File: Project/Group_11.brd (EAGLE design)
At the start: 100 x 80 mm, 29 parts, among them J1 POWER_JACKPTH_LOCK, U1 +12v

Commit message: Modifica symbols e schematico aggiornato
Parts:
- moved R1 61.4 mm to (20.3, 20.3)
- moved D1 56.2 mm to (21.6, 24.1)
- moved R11 36.1 mm to (38.1, 22.9), turned to 90 degrees
- moved U2 35.8 mm to (43.2, 21.6)
- moved R10 34.2 mm to (33.0, 22.9), turned to 180 degrees
- moved R6 29.2 mm to (49.5, 55.9), turned to 180 degrees
- moved U$3 21.7 mm to (33.0, 63.5), turned to 0 degrees
- moved U$1 21.6 mm to (63.5, 67.3)
- moved R8 19.8 mm to (52.1, 71.1)
- moved R5 18.1 mm to (2.54, 44.5), turned to 270 degrees
- moved J6 17.3 mm to (68.6, 22.9)
- moved U$2 17.3 mm to (50.8, 39.4)
- moved R9 12.7 mm to (10.2, 44.5)
- moved S1 10.2 mm to (62.2, 14.0)
- moved C1 9.92 mm to (40.6, 11.4)
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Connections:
- new net N$17: J6.1, U$2.32
- new net N$18: C3.2, U$3.12
- net 5V: now also R2.2, R3.2, R8.2, R9.2; no longer R2.1, R3.1, R8.1, R9.1
- net GND: no longer C3.2, U$3.12
- net I2C_SCL_0: now also R2.1; no longer R2.2
- net I2C_SCL_1: now also R8.1; no longer R8.2
- net I2C_SDA: no longer J6.1, U$2.32
- net I2C_SDA_0: now also R3.1; no longer R3.2
- net I2C_SDA_1: now also R9.1; no longer R9.2
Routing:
- net PHOTO_OUT: track 0.00 -> 7.66 mm
- net TEMP_OUT: track 0.00 -> 5.50 mm
- net N$7: track 0.00 -> 5.08 mm
- net N$5: track 0.00 -> 5.08 mm
- net N$17: track 0.00 -> 5.08 mm
- net N$8: track 0.00 -> 4.83 mm
- net N$6: track 0.00 -> 4.83 mm
- net N$4: track 0.00 -> 4.83 mm
- net N$2: track 0.00 -> 4.24 mm
- net N$3: track 0.00 -> 3.91 mm

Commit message: Aggiornamento board
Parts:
- moved J2 62.2 mm to (78.7, 58.4), turned to 271.5 degrees
- moved C2 57.5 mm to (55.9, 17.8)
- moved J3 32.4 mm to (50.8, 61.0), turned to 90 degrees
- moved U1 31.9 mm to (52.1, 10.2)
- moved R5 27.4 mm to (27.9, 54.6)
- moved R9 26.2 mm to (34.3, 54.6)
- moved J7 26.2 mm to (61.0, 53.3)
- moved R4 25.4 mm to (73.7, 62.2)
- moved R3 24.4 mm to (73.7, 58.4)
- moved R7 24.1 mm to (54.6, 54.6), turned to 270 degrees
- moved R2 22.7 mm to (73.7, 54.6), turned to 180 degrees
- moved J8 21.6 mm to (24.1, 61.0)
- moved J5 18.1 mm to (61.0, 59.7), turned to 270 degrees
- moved J4 17.3 mm to (61.0, 66.0), turned to 270 degrees
- moved C1 13.5 mm to (49.5, 21.6)
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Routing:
- net PHOTO_OUT: track 7.66 -> 10.6 mm
- net TEMP_OUT: track 5.50 -> 8.04 mm
- net N$2: track 4.24 -> 2.31 mm
- added copper zone on layer 1, net GND

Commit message: Aggiornamento parte inferiore
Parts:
- moved U1 62.4 mm to (47.0, 72.4)
- moved C2 58.4 mm to (54.6, 76.2)
- moved S1 54.6 mm to (63.5, 72.4)
- moved J1 54.6 mm to (88.9, 72.4)
- moved C3 53.3 mm to (31.8, 67.3)
- moved C1 46.6 mm to (40.6, 67.3)
- moved J8 18.2 mm to (40.6, 53.3), turned to 180 degrees
- moved J7 15.3 mm to (45.7, 54.6)
- moved U$3 9.67 mm to (33.0, 58.4), turned to 0 degrees
- moved R5 8.52 mm to (31.8, 62.2)
- moved R9 8.13 mm to (39.4, 61.0)
- moved R10 7.73 mm to (39.4, 22.9), turned to 180 degrees
- moved R1 7.62 mm to (29.2, 21.6), turned to 180 degrees
- moved U2 6.84 mm to (49.5, 21.6)
- moved R11 6.35 mm to (44.5, 22.9)
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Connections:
- removed net N$18: C3.2, U$3.12
- net GND: now also C3.2, U$3.12
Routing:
- net PHOTO_OUT: track 10.6 -> 0.00 mm
- net TEMP_OUT: track 8.04 -> 0.00 mm
- net N$7: track 5.08 -> 0.00 mm
- net N$5: track 5.08 -> 0.00 mm
- net N$17: track 5.08 -> 0.00 mm
- net N$8: track 4.83 -> 0.00 mm
- net N$6: track 4.83 -> 0.00 mm
- net N$4: track 4.83 -> 0.00 mm
- net N$3: track 3.91 -> 0.00 mm
- net N$2: track 2.31 -> 0.00 mm
- added copper zone on layer 16, net 5V

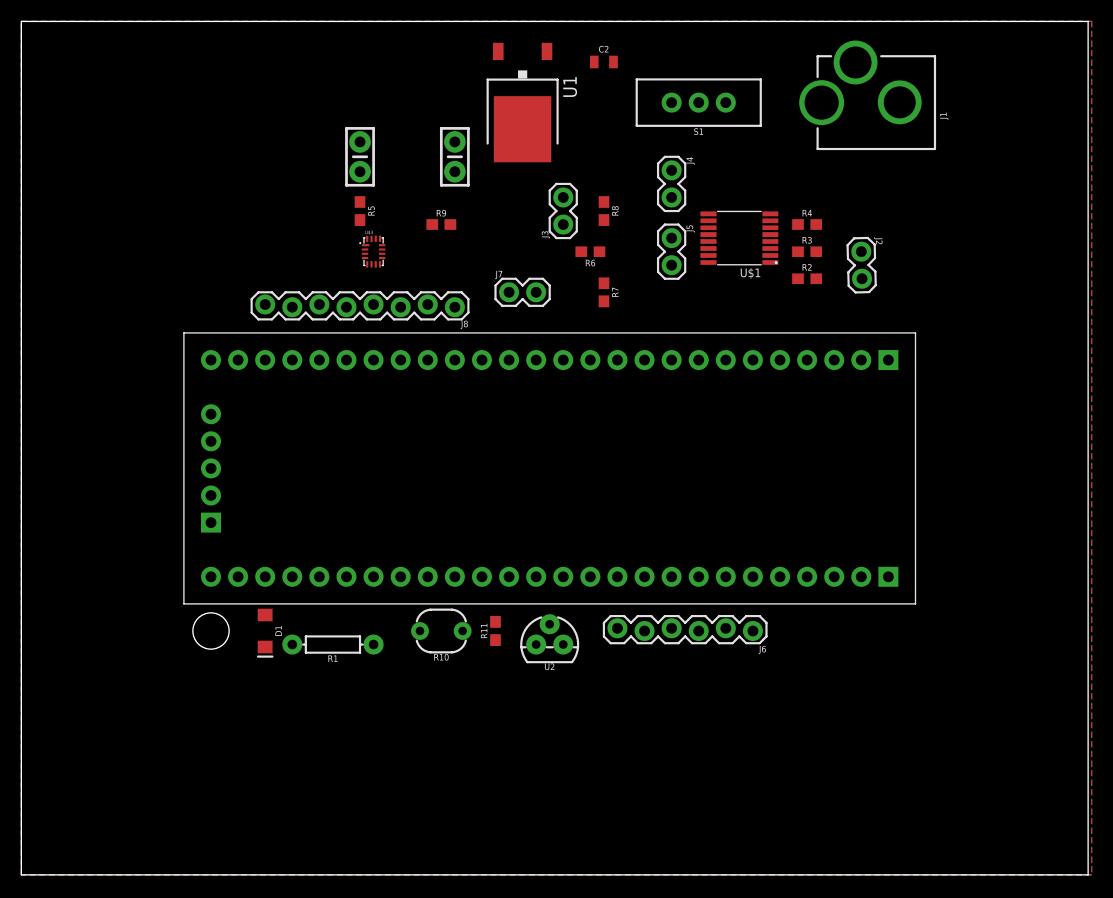
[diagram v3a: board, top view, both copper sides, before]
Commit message: Prova disposizione board
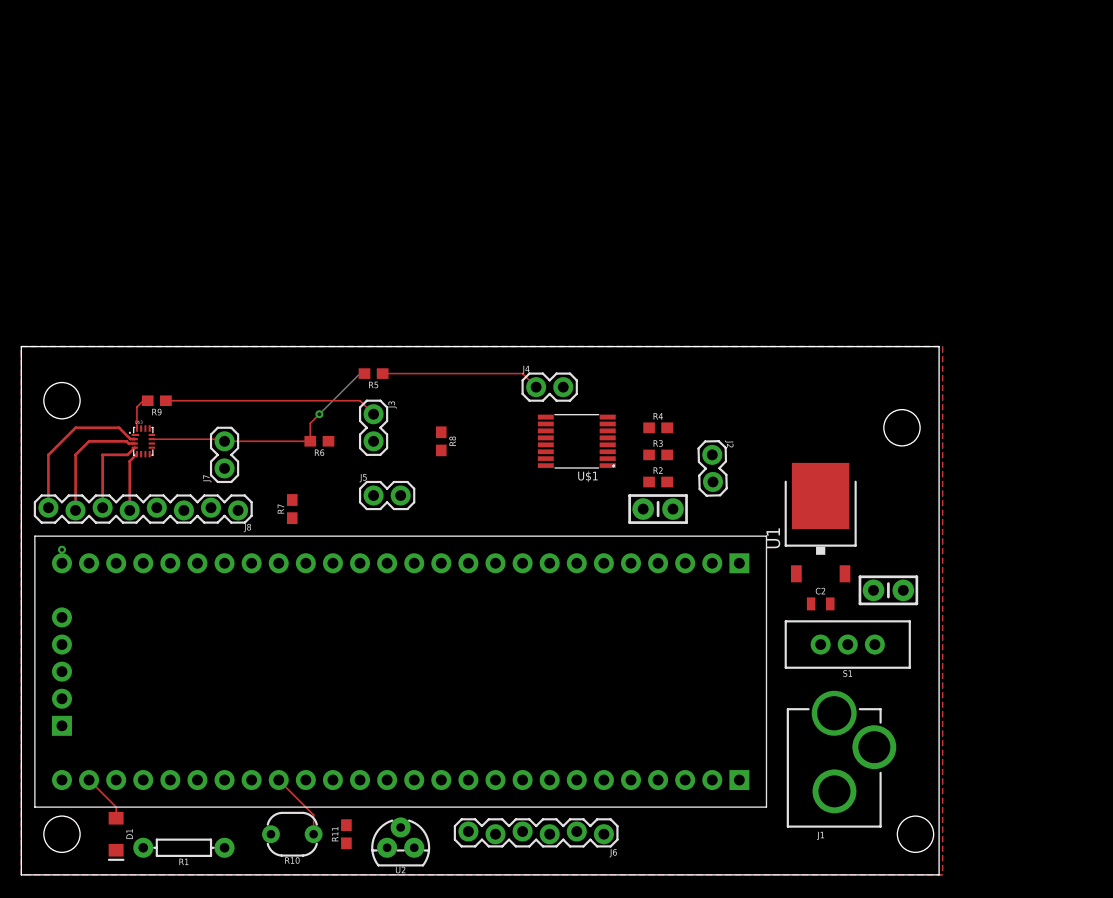
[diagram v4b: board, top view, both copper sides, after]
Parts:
- moved J1 72.2 mm to (76.2, 1.27), turned to 0 degrees
- moved C1 57.5 mm to (81.3, 26.7), turned to 0 degrees
- moved C2 54.7 mm to (74.9, 25.4)
- moved S1 52.7 mm to (77.5, 21.6)
- moved U1 48.3 mm to (74.9, 33.0), turned to 0 degrees
- moved C3 43.3 mm to (59.7, 34.3), turned to 0 degrees
- moved J5 36.9 mm to (33.0, 35.6), turned to 0 degrees
- moved R7 35.6 mm to (25.4, 34.3), turned to 90 degrees
- moved J7 31.4 mm to (19.1, 38.1), turned to 90 degrees
- moved R9 31.4 mm to (12.7, 44.5), turned to 180 degrees
- moved R6 31.0 mm to (27.9, 40.6)
- moved U$3 28.0 mm to (11.4, 40.6)
- moved J8 27.9 mm to (20.3, 34.3)
- moved R8 26.4 mm to (39.4, 40.6)
- moved J3 25.1 mm to (33.0, 43.2), turned to 270 degrees
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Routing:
- net 5V: track 0.00 -> 27.7 mm, vias 0 -> 2
- net I2C_SDA_1: track 0.00 -> 20.0 mm
- net I2C_SDA_2: track 0.00 -> 14.9 mm
- net N$1: track 0.00 -> 14.5 mm
- net N$10: track 0.00 -> 11.4 mm
- net N$16: track 0.00 -> 8.24 mm
- net PHOTO_OUT: track 0.00 -> 6.43 mm
- net N$15: track 0.00 -> 5.55 mm
- net N$3: track 0.00 -> 4.63 mm
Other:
- board size 100 x 80 mm -> 86 x 49.5 mm
